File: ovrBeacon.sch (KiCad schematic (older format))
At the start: 48 parts, among them J1 USB_MICROB_RA, J2 CONN_DBG_PDI, J3 CONN_2MM_9, Q1 FET_NP_5A/3A_60V, T1 THERM_NTC_10K_0603, U1 MICROCHIP_MCP73831, U10 WORLDSEMI_WS2812, U11 WORLDSEMI_WS2812, U12 WORLDSEMI_WS2812, U2 BLUEGIGA_BLE113, U3 TI_TPS62730, U4 WORLDSEMI_WS2812, U5 WORLDSEMI_WS2812, U6 WORLDSEMI_WS2812, U7 WORLDSEMI_WS2812, U8 TOSHIBA_TCS40DLR, U9 WORLDSEMI_WS2812

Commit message: initial commit of version 0.3…passed DFM, waiting for manufacture review
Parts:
- removed C11, C13, C14, C6, C7, C8: C_0.1uF_10v_0603, ovrEngineered:C_0603, symbol C_0.1uF_10v_0603
- removed C4, C5: C_2.2uF_10v_0603, ovrEngineered:C_0603, symbol C_2.2uF_10v_0603
- removed C9: C_0.47uF_10v_0603, ovrEngineered:C_0603, symbol C_0.47uF_10v_0603
- removed D1: LED_GREEN_0603, ovrEngineered:D_0603, symbol LED_GREEN_0603
- removed D2: LED_RED_0603, ovrEngineered:D_0603, symbol LED_RED_0603
- removed J1: USB_MICROB_RA, ovrEngineered:USB_MICROB_RA, symbol USB_MICROB_RA
- removed J2: CONN_DBG_PDI, ovrEngineered:TC2030-IDC, symbol CONN_DBG_PDI
- removed J3: CONN_2MM_9, ovrEngineered:SIP_2MM_9, symbol CONN_2MM_9
- removed L1: I_2.2uH_20%_0603, ovrEngineered:R_0603, symbol I_2.2uH_20%_0603
- removed Q1: FET_NP_5A/3A_60V, ovrEngineered:SO-8, symbol FET_NP_5A/3A_60V
- removed R11, R17: R_402_1%_0603, ovrEngineered:R_0603, symbol R_402_1%_0603
- removed R12, R15, R16, R6, R7: R_10K_1%_0603, ovrEngineered:R_0603, symbol R_10K_1%_0603
- removed R13, R14, R8: R_15K_1%_0603, ovrEngineered:R_0603, symbol R_15K_1%_0603
- removed R3: R_2K_1%_0603, ovrEngineered:R_0603, symbol R_2K_1%_0603
- removed R4, R5: R_5.1K_1%_0603, ovrEngineered:R_0603, symbol R_5.1K_1%_0603
- removed T1: THERM_NTC_10K_0603, ovrEngineered:R_0603, symbol THERM_NTC_10K_0603
- removed U1: MICROCHIP_MCP73831, ovrEngineered:SOT-23-5, symbol MICROCHIP_MCP73831
- removed U10, U11, U12, U4, U5, U6, U7, U9: WORLDSEMI_WS2812, ovrEngineered:WS2812, symbol WORLDSEMI_WS2812
- removed U3: TI_TPS62730, ovrEngineered:TPS62730, symbol TI_TPS62730
- removed U8: TOSHIBA_TCS40DLR, ovrEngineered:SOT-23-3, symbol TOSHIBA_TCS40DLR
- added C1: C_0.15uF_25v_0603, ovrEngineered:C_0603, symbol C_0.15uF_25v_0603
- added C11, C13: C_1uF_10v_0805, ovrEngineered:C_0805, symbol C_1uF_10v_0805
- added C2: C_2200pF_50v_0603, ovrEngineered:C_0603, symbol C_2200pF_50v_0603
- added C3, C8: C_0.47uF_25v_0603, ovrEngineered:C_0603, symbol C_0.47uF_25v_0603
- added C4, C7: C_0.022uF_25v_0603, ovrEngineered:C_0603, symbol C_0.022uF_25v_0603
- added C5, C6: C_10000pF_25v_0603, ovrEngineered:C_0603, symbol C_10000pF_25v_0603
- added C9: C_22uF_25v_0805, ovrEngineered:C_0805, symbol C_22uF_25v_0805
- added D1, D2: CREE_CLV1A_FKB, ovrEngineered:CREE_CLV1A_FKB, symbol CREE_CLV1A_FKB
- added J1: CONN_1.27MM_5X2, ovrEngineered:20021111-00010T4LF, symbol CONN_1.27MM_5X2
- added J2: CONN_2MM_2, ovrEngineered:SIP_2MM_2, symbol CONN_2MM_2
- added L1: QIRX_10.7uH, ovrEngineered:SIP_2MM_2, symbol QIRX_10.7uH
- added R11: R_12K_1%_0603, ovrEngineered:R_0603, symbol R_12K_1%_0603
- added R12: R_5.1K_1%_0603, ovrEngineered:R_0603, symbol R_5.1K_1%_0603
- added R14, R15, R16, R17, R18, R19: R_120_1%_0603, ovrEngineered:R_0603, symbol R_120_1%_0603
- added R3: R_953_1%_0603, ovrEngineered:R_0603, symbol R_953_1%_0603
- added R4, R5: R_10K_1%_0603, ovrEngineered:R_0603, symbol R_10K_1%_0603
- added R6, R7: R_300_1%_0603, ovrEngineered:R_0603, symbol R_300_1%_0603
- added R8: R_42.2K_1%_0603, ovrEngineered:R_0603, symbol R_42.2K_1%_0603
- added U2: TI_BQ51050, ovrEngineered:TI_BQ51050, symbol TI_BQ51050
- added U3: TOREX_XC6210, ovrEngineered:SOT-25-5, symbol TOREX_XC6210
- added U4: NXP_PCA9624, ovrEngineered:NXP_PCA9624, symbol NXP_PCA9624
- added U5: LITEON_LTR-329ALS, ovrEngineered:LITEON_LTR-329ALS, symbol LITEON_LTR-329ALS
- added U6: SILICONLABS_SI7050, symbol SILICONLABS_SI7050
- added U7: ANALOGDEVS_ADXL345, ovrEngineered:ANALOGDEVS_ADXL345, symbol ANALOGDEVS_ADXL345
- renumbered U2 to U1
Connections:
- net +BATT: now also C13.1, J2.2, R11.1, U2.11 (EN2), U2.4 (BATT), U3.1 (VIN), U3.3 (CE); no longer C10.1, R10.2
- net GND: now also C11.2, C13.2, C9.2, J1.1, J2.1, R12.2, R3.2, R5.2, R6.2, U2.1 (GND), U2.20 (GND), U2.21 (PAD), U2.9 (AD), U3.2 (GND), U4.10 (GND), U4.15 (GND), U4.17 (A5), U4.18 (A6), U4.22 (GND), U4.25 (PAD), U4.3 (A4), U4.4 (GND), U4.9 (GND), U5.2 (GND), U6.2 (GND), U7.2 (GND), U7.4 (GND), U7.5 (GND); no longer R9.2
- net P2_1/PROG: now also J1.4
- net P2_2/PROG: now also J1.3
- net ~RESET: now also J1.7
- net SCL: now reaches U1.14 (SCL)
- net SCL: now also R10.2, U4.19 (SCL), U5.4 (SCL), U6.6 (SCL), U7.14 (SCL/SCK)
- net SDA: now reaches U1.15 (SDA)
- net SDA: now also R9.2, U4.20 (SDA), U5.3 (SDA), U6.1 (SDA), U7.13 (SDA/SDI/SDO)
- net ~CHARGING: now reaches U1.24 (P1_0)
- net ~CHARGING: now also R4.2, U2.7 (~CHG)
- net +3V3: now reaches R10.1
- net +3V3: now also C10.1, R1.1, R9.1, U1.17 (DVCC), U1.8 (AVCC), C11.1, D1.2 (ANODE), D2.2 (ANODE), J1.2, R4.1, U3.5 (VOUT), U4.1 (A2), U4.2 (A3), U4.21 (VCC), U4.23 (A0), U4.24 (A1), U5.1 (VCC), U6.5 (VCC), U7.1 (VDDIO), U7.12 (SDO/ALTADDR), U7.6 (VCC), U7.7 (~CS)
- net CHARGING renamed ACC_INT1
- net ACC_INT1: now also U7.8 (INT1)
- net CHARGING_STAT renamed ~LED_EN
- net ~LED_EN: now also U4.16 (~OE)
- net DCDC: no longer names the net of U1.13 (P1_6)
- net DCDC: no longer R9.1
- net EXT_POWER renamed ACC_INT2
- net ACC_INT2: now also U7.9 (INT2)
- net NEOPIXELS renamed VBATT
- net VBATT: now also R11.2, R12.1
- net SW_ENUM: no longer names the net of U1.21 (P1_3)
- net THERM_EXT_1: no longer names the net of U1.11 (P2_0)
- net THERM_EXT_1: no longer U1.31 (P0_2)
- net THERM_EXT_2: no longer names the net of U1.12 (P1_7)
- net THERM_EXT_2: no longer U1.30 (P0_3)
- net THERM_INT: no longer names the net of U1.27 (P0_6)
- net TIMER1_CC0/ADC: no longer names the net of U1.22 (P1_2)
- net TIMER1_CC0/ADC: no longer U1.26 (P0_7)
- net USART_TX: no longer names the net of U1.29 (P0_4)
- removed net VCC: R1.1, U1.17 (DVCC), U1.28 (P0_5), U1.8 (AVCC)
- new net: C1.1, L1.1
- new net: C1.2, C2.1, C3.1, C4.1, C5.1, U2.2 (AC1)
- new net: C2.2, C6.1, C7.1, C8.1, L1.2, U2.19 (AC2)
- new net: C6.2, U2.17 (BOOT2)
- new net: C5.2, U2.3 (BOOT1)
- new net: C3.2, U2.5 (CLAMP1)
- new net: C8.2, U2.16 (CLAMP2)
- new net: C4.2, U2.6 (COMM1)
- new net: C7.2, U2.15 (COMM2)
- new net: C9.1, R8.1, U2.18 (RECT)
- new net: R6.1, R7.1, R8.2, U2.14 (FOD)
- new net: R7.2, U2.12 (ILIM)
- new net: R3.1, U2.10 (TERM)
- new net: R5.1, U2.13 (TS/CTRL)
- new net: R14.1, U4.5 (LED0)
- new net: D1.1 (CATHODE_RED), R14.2
- new net: R15.1, U4.6 (LED1)
- new net: D1.4 (CATHOD_GREEN), R15.2
- new net: R16.1, U4.7 (LED2)
- new net: D1.3 (CATHODE_BLUE), R16.2
- new net: R17.1, U4.12 (LED5)
- new net: D2.1 (CATHODE_RED), R17.2
- new net: R18.1, U4.13 (LED6)
- new net: D2.4 (CATHOD_GREEN), R18.2
- new net: R19.1, U4.14 (LED7)
- new net: D2.3 (CATHODE_BLUE), R19.2
- no-connect marks 8 -> 20
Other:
- note added: "Accelerometer"
- note added: "Battery"
- note added: "Bulk Caps"
- note added: "I2C ADDR (7-bit): 0x0F\nI2C ADDR (8-bit): 0x1E"
- note added: "I2C ADDR (7-bit): 0x1D\nI2C ADDR (8-bit): 0x3A"
- note added: "I2C ADDR (7-bit): 0x29\nI2C ADDR (8-bit): 0x52"
- note added: "I2C ADDR (7-bit): 0x40\nI2C ADDR (8-bit): 0x80"
- note added: "I2C Pull-ups"
- note added: "LED Controller"
- note added: "Light Sensor"
- note added: "Temp Sensor"
- note added: "Voltage Regulator"
- note added: "Wireless Charger"
- note removed: "Charging"
- note removed: "Enumeration Switch (magnetic)"
- note removed: "External Power / TimerCC / ADC"
- note removed: "NeoPixels"
- note removed: "P2_0, P1_7 pass-through for better routing"
- note removed: "Radio Regulator"
- note removed: "Rprog(kO) = 1000V / Ireg(mA)\n2K = 1000V / 500mA"
- moved on the sheet: R1, R2, U1

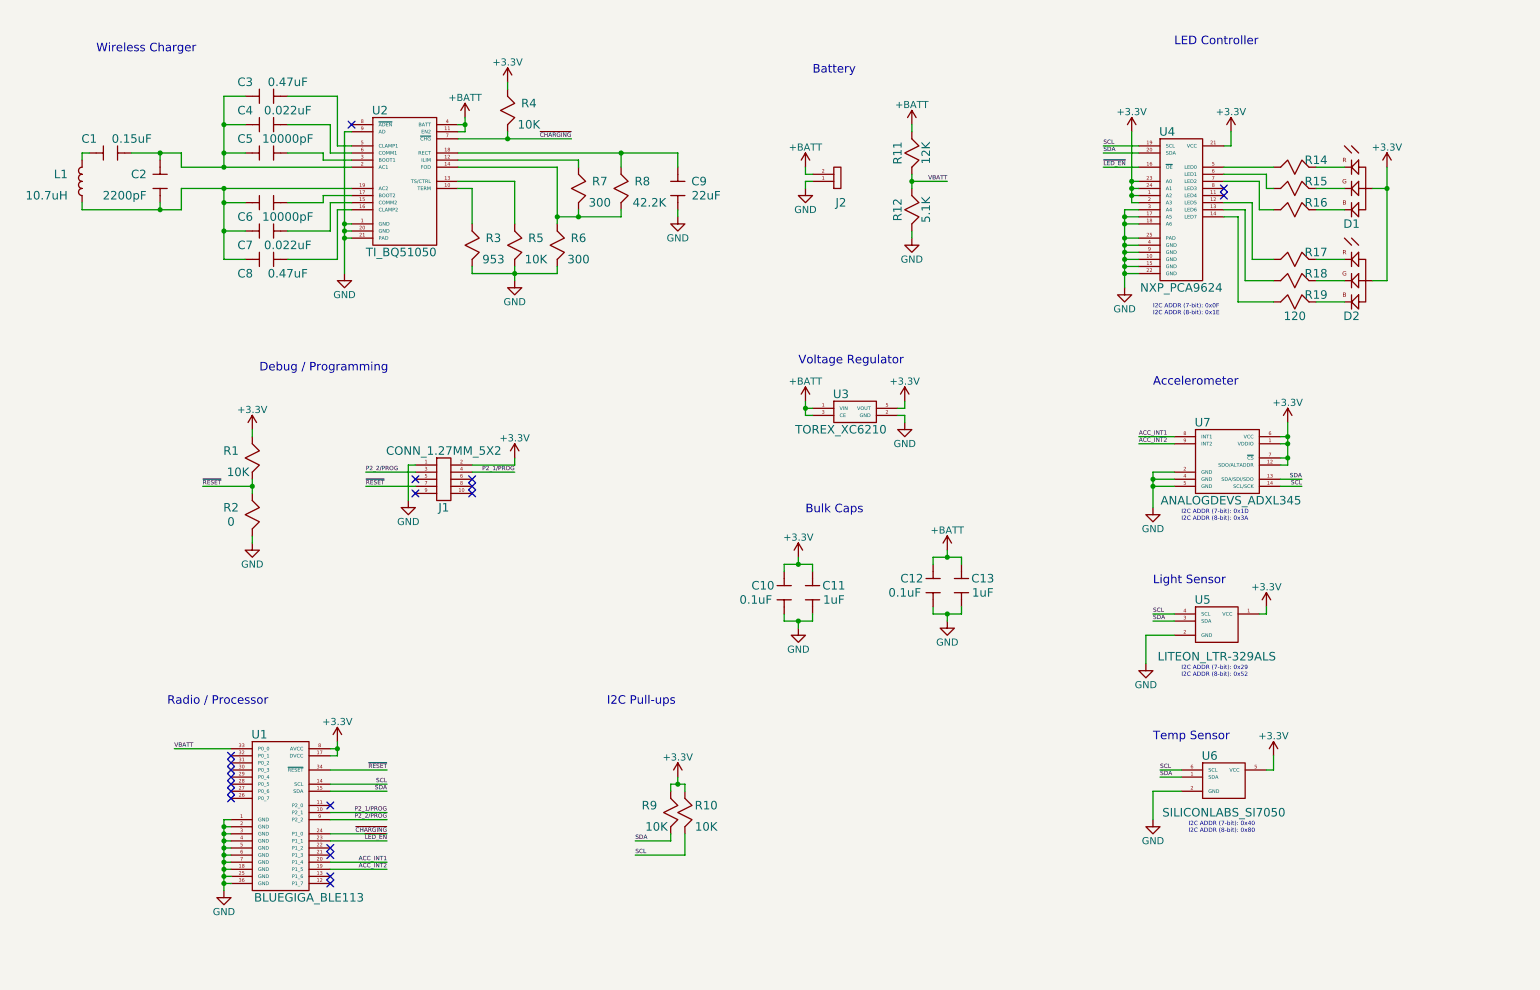
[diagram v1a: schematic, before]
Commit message: Fixed redlines from v0.3, added fiducials for pick and place…getting ready to start adjusting component centers for pick and place
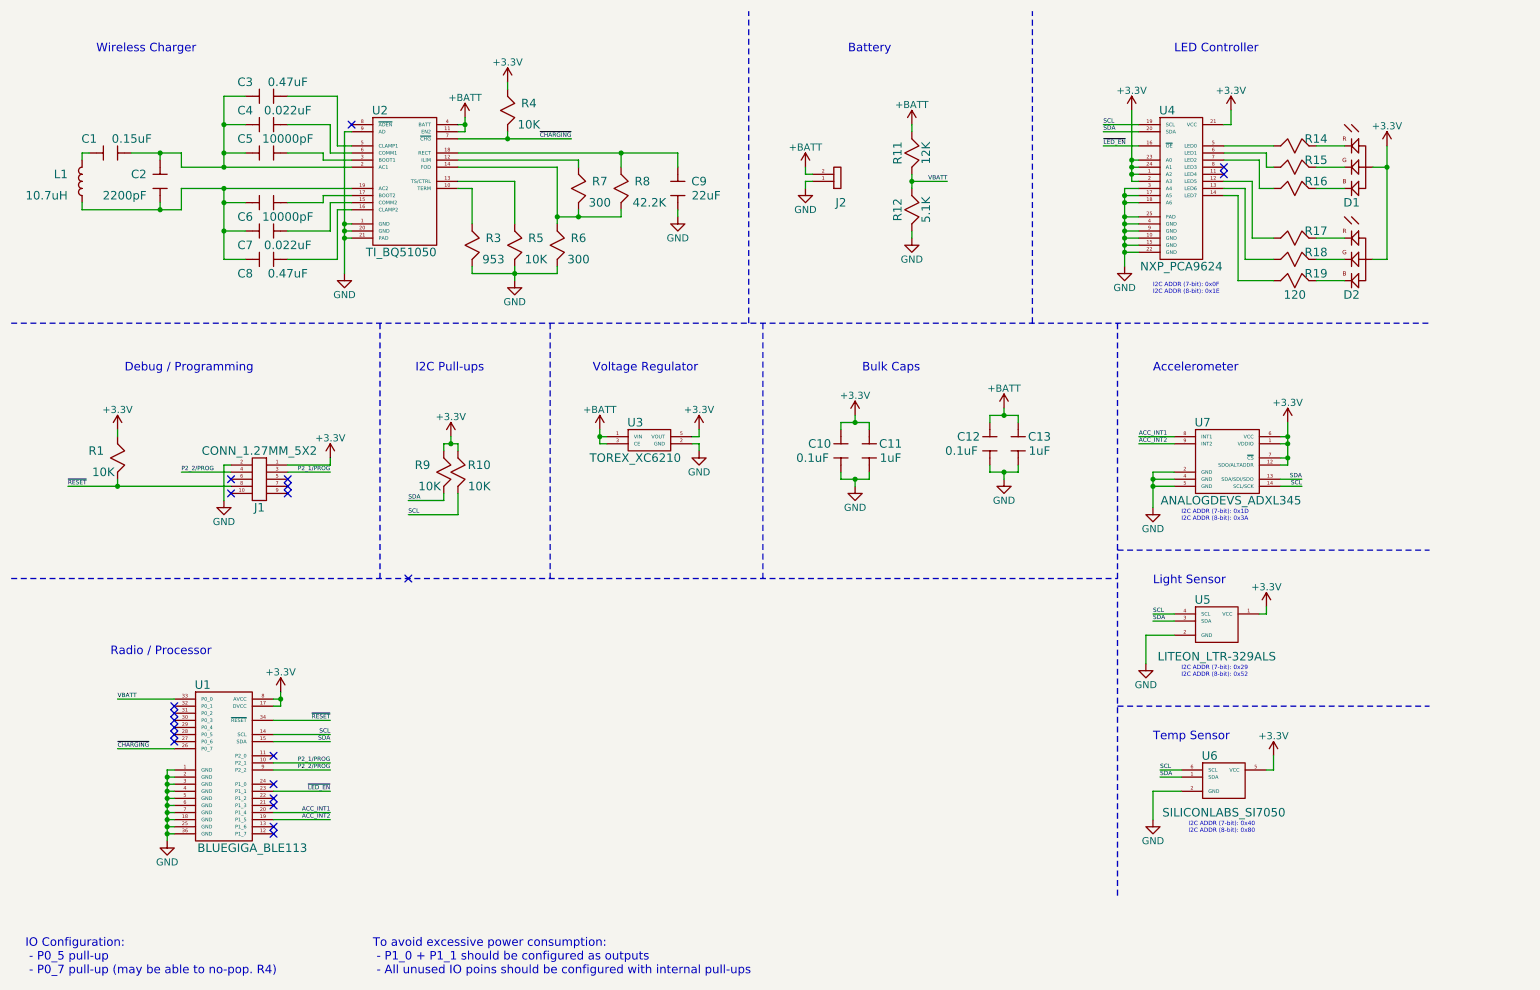
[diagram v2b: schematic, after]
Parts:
- removed R2: R_0_0603, ovrEngineered:R_0603, symbol R_0_0603
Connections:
- net +3V3: now also J1.1; no longer J1.2
- net GND: now also J1.2; no longer J1.1
- net P2_1/PROG: now also J1.3; no longer J1.4
- net P2_2/PROG: now also J1.4; no longer J1.3
- net ~CHARGING: now also U1.26 (P0_7); no longer U1.24 (P1_0)
- net ~RESET: now also J1.8; no longer J1.7
- no-connect marks 20 -> 21
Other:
- note added: "IO Configuration:\n - P0_5 pull-up\n - P0_7 pull-up (may be able to no-pop. R4)"
- note added: "To avoid excessive power consumption:\n - P1_0 + P1_1 should be configured as outputs\n - All unused IO poins should be configured with internal pull-ups"
- moved on the sheet: C10, C11, C12, C13, D1, D2, J1, R1, R10, R14, R15, R16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
